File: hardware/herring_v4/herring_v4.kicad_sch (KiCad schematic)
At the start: 7 parts, among them U1 W65C02, U2 AS6C62256, U3 AT28C64B, U4 W65C51, U5 ATF16V8B, X1 CXO_DIP14, X2 CXO_DIP8

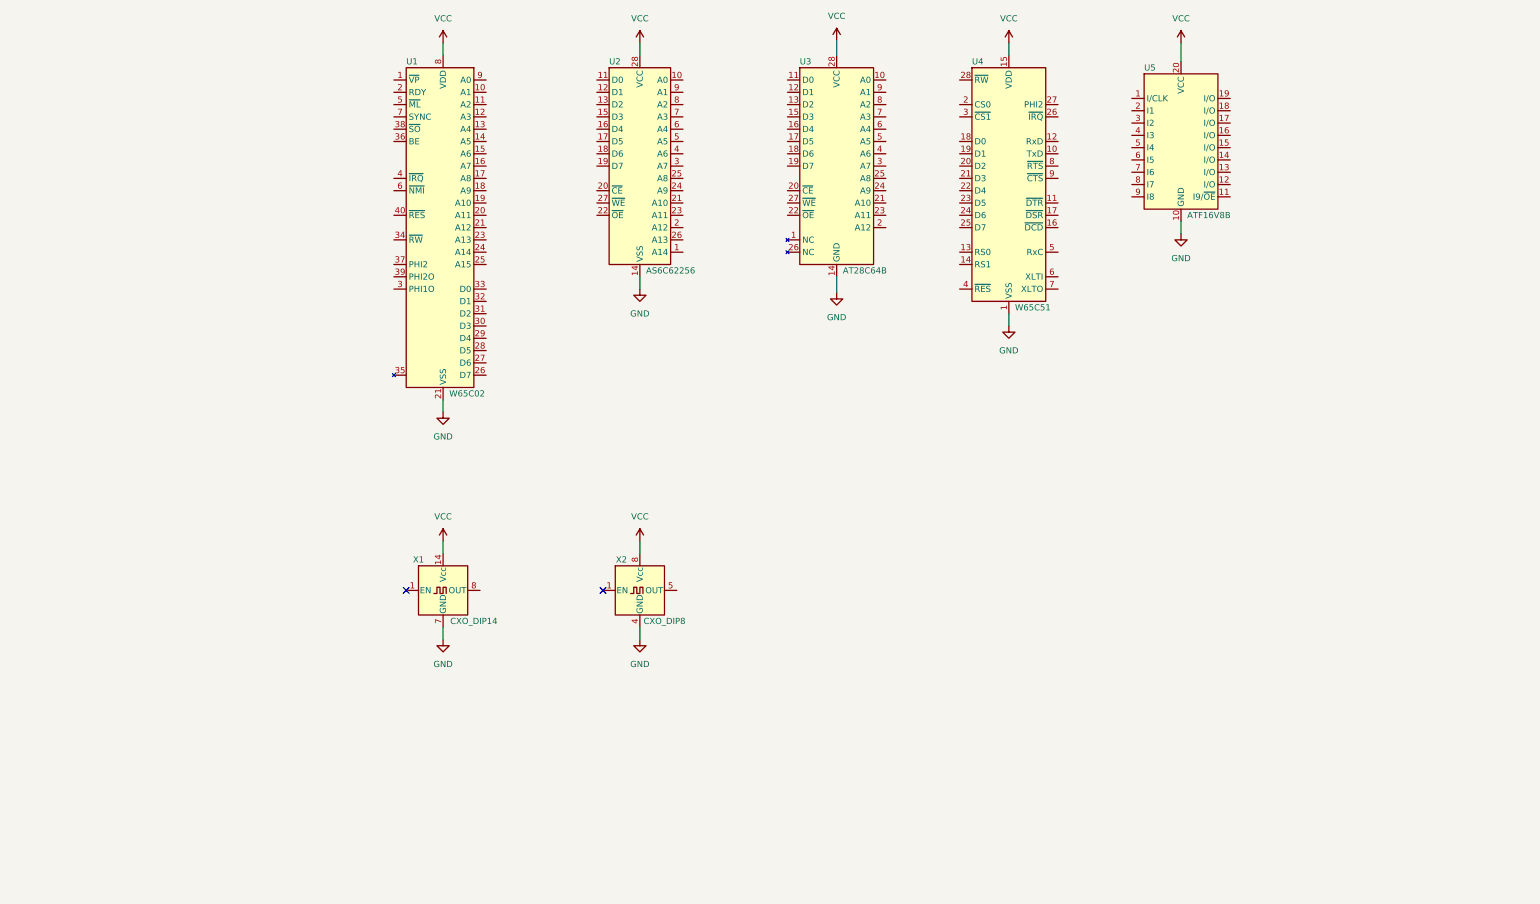
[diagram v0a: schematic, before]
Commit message: Add 16C550 to schematic
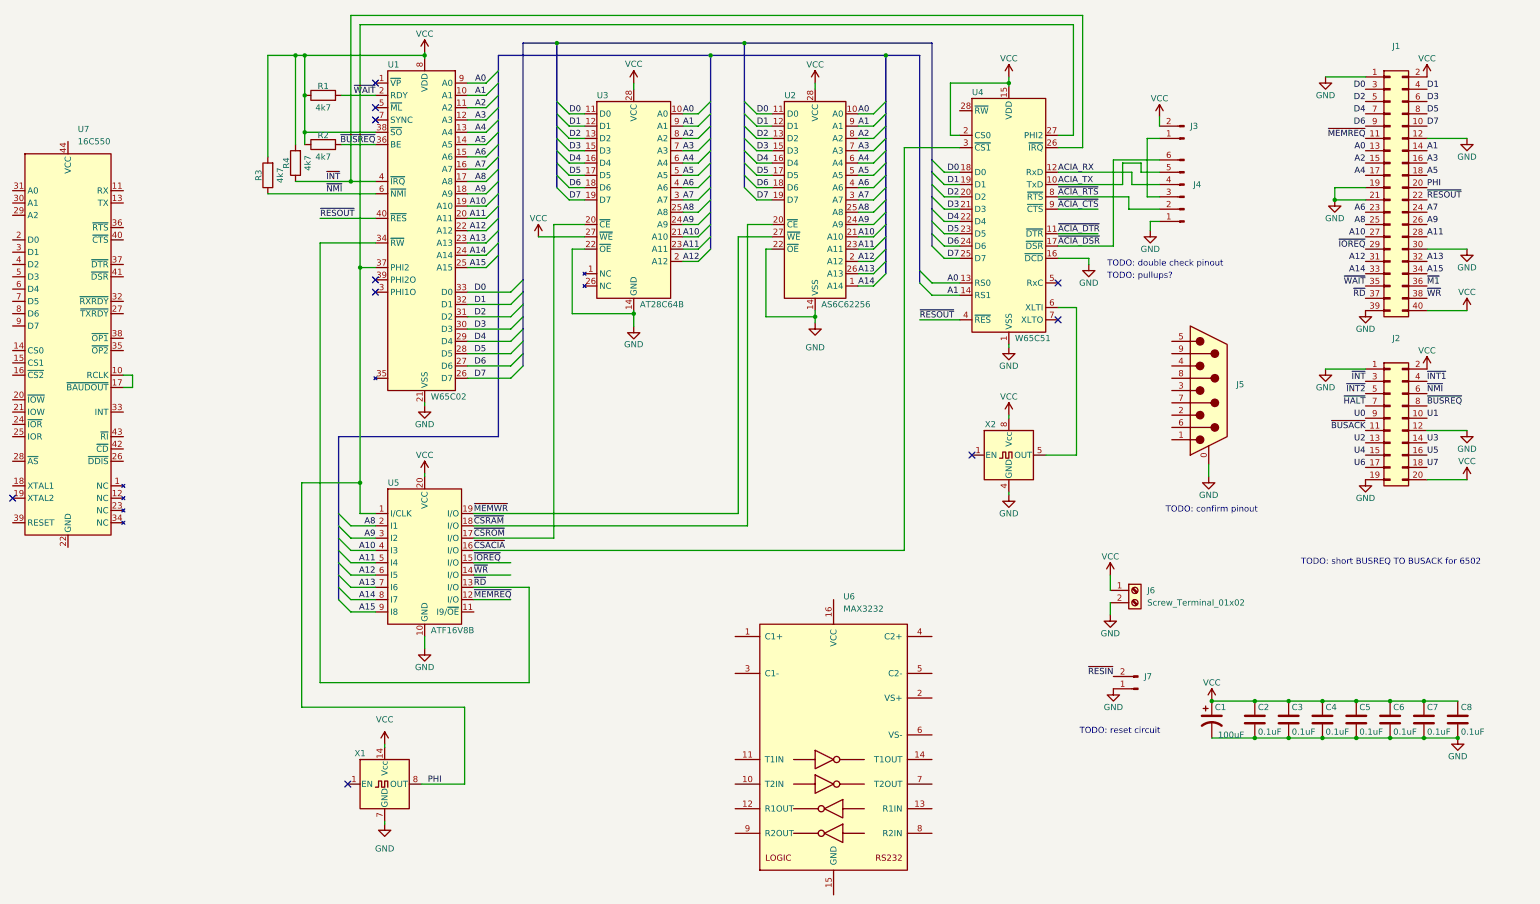
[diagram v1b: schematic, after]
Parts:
- added C1: 100uF, Capacitor_THT:CP_Radial_D8.0mm_P3.50mm, symbol Device:C_Polarized_US
- added C2, C3, C4, C5, C6, C7, C8: 0.1uF, Capacitor_THT:C_Disc_D5.0mm_W2.5mm_P5.00mm, symbol Device:C
- added J1: Conn_02x20_Odd_Even, Connector_PinSocket_2.54mm:PinSocket_2x21_P2.54mm_Horizontal, symbol Connector_Generic:Conn_02x20_Odd_Even
- added J2: Conn_02x10_Odd_Even, Connector_PinSocket_2.54mm:PinSocket_2x10_P2.54mm_Horizontal, symbol Connector_Generic:Conn_02x10_Odd_Even
- added J3, J7: Conn_01x02_Male, Connector_PinHeader_2.54mm:PinHeader_1x02_P2.54mm_Vertical, symbol Connector:Conn_01x02_Male
- added J4: Conn_01x06_Male, Connector_PinHeader_2.54mm:PinHeader_1x06_P2.54mm_Vertical, symbol Connector:Conn_01x06_Male
- added J5: DB9_Male_MountingHoles, Connector_Dsub:DSUB-9_Male_Horizontal_P2.77x2.84mm_EdgePinOffset7.70mm_Housed_MountingHolesOffset9.12mm, symbol Connector:DB9_Male_MountingHoles
- added J6: Screw_Terminal_01x02, TerminalBlock:TerminalBlock_bornier-2_P5.08mm, symbol Connector:Screw_Terminal_01x02
- added R1, R2, R3, R4: 4k7, Resistor_THT:R_Axial_DIN0207_L6.3mm_D2.5mm_P10.16mm_Horizontal, symbol Device:R
- added U6: MAX3232, Package_DIP:DIP-16_W7.62mm_Socket, symbol Interface_UART:MAX3232
- added U7: 16C550, Package_LCC:PLCC-44_THT-Socket, symbol herring:16C550
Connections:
- net GND: now also U2.22 (~{OE}), U3.22 (~{OE}), U4.16 (~{DCD}), C1.2, C2.2, C3.2, C4.2, C5.2, C6.2, C7.2, C8.2, J1.1 (Pin_1), J1.12 (Pin_12), J1.19 (Pin_19), J1.21 (Pin_21), J1.30 (Pin_30), J1.39 (Pin_39), J2.1 (Pin_1), J2.12 (Pin_12), J2.19 (Pin_19), J4.1 (Pin_1), J5.0 (PAD), J6.2 (Pin_2), J7.1 (Pin_1)
- net VCC: now also U1.38 (~{SO}), U3.27 (~{WE}), U4.2 (CS0), C1.1, C2.1, C3.1, C4.1, C5.1, C6.1, C7.1, C8.1, J1.2 (Pin_2), J1.40 (Pin_40), J2.2 (Pin_2), J2.20 (Pin_20), J3.2 (Pin_2), J6.1 (Pin_1), R1.1, R2.1, R3.2, R4.2
- net at X2.5 (OUT): now also U4.6 (XLTI)
- net PHI: now reaches U5.1 (I/CLK)
- net PHI: now also U1.37 (PHI2), U4.27 (PHI2), X1.8 (OUT), J1.20 (Pin_20)
- net ~{MEMREQ}: now reaches U5.12 (I/O)
- net ~{MEMREQ}: now also J1.11 (Pin_11)
- net ~{RD}: now reaches U5.13 (I/O)
- net ~{RD}: now also U1.34 (~{RW}), J1.37 (Pin_37)
- net ~{WR}: now reaches U5.14 (I/O)
- net ~{WR}: now also J1.38 (Pin_38)
- net ~{IOREQ}: now reaches U5.15 (I/O)
- net ~{IOREQ}: now also J1.29 (Pin_29)
- net ~{CSACIA}: now reaches U5.16 (I/O)
- net ~{CSACIA}: now also U4.3 (~{CS1})
- net ~{CSROM}: now reaches U5.17 (I/O)
- net ~{CSROM}: now also U3.20 (~{CE})
- net ~{CSRAM}: now reaches U5.18 (I/O)
- net ~{CSRAM}: now also U2.20 (~{CE})
- net ~{MEMWR}: now reaches U5.19 (I/O)
- net ~{MEMWR}: now also U2.27 (~{WE})
- net A8: now reaches U5.2 (I1)
- net A8: now also U1.17 (A8), U2.25 (A8), U3.25 (A8), J1.25 (Pin_25)
- net A9: now reaches U5.3 (I2)
- net A9: now also U1.18 (A9), U2.24 (A9), U3.24 (A9), J1.26 (Pin_26)
- net A10: now reaches U5.4 (I3)
- net A10: now also U1.19 (A10), U2.21 (A10), U3.21 (A10), J1.27 (Pin_27)
- net A11: now reaches U5.5 (I4)
- net A11: now also U1.20 (A11), U2.23 (A11), U3.23 (A11), J1.28 (Pin_28)
- net A12: now reaches U5.6 (I5)
- net A12: now also U1.22 (A12), U2.2 (A12), U3.2 (A12), J1.31 (Pin_31)
- net A13: now reaches U5.7 (I6)
- net A13: now also U1.23 (A13), U2.26 (A13), J1.32 (Pin_32)
- net A14: now reaches U5.8 (I7)
- net A14: now also U1.24 (A14), U2.1 (A14), J1.33 (Pin_33)
- net A15: now reaches U5.9 (I8)
- net A15: now also U1.25 (A15), J1.34 (Pin_34)
- net A0: now reaches U2.10 (A0)
- net A0: now also U1.9 (A0), U3.10 (A0), U4.13 (RS0), J1.13 (Pin_13)
- net D0: now reaches U2.11 (D0)
- net D0: now also U1.33 (D0), U3.11 (D0), U4.18 (D0), J1.3 (Pin_3)
- net D1: now reaches U2.12 (D1)
- net D1: now also U1.32 (D1), U3.12 (D1), U4.19 (D1), J1.4 (Pin_4)
- net D2: now reaches U2.13 (D2)
- net D2: now also U1.31 (D2), U3.13 (D2), U4.20 (D2), J1.5 (Pin_5)
- net D3: now reaches U2.15 (D3)
- net D3: now also U1.30 (D3), U3.15 (D3), U4.21 (D3), J1.6 (Pin_6)
- net D4: now reaches U2.16 (D4)
- net D4: now also U1.29 (D4), U3.16 (D4), U4.22 (D4), J1.7 (Pin_7)
- net D5: now reaches U2.17 (D5)
- net D5: now also U1.28 (D5), U3.17 (D5), U4.23 (D5), J1.8 (Pin_8)
- net D6: now reaches U2.18 (D6)
- net D6: now also U1.27 (D6), U3.18 (D6), U4.24 (D6), J1.9 (Pin_9)
- net D7: now reaches U2.19 (D7)
- net D7: now also U1.26 (D7), U3.19 (D7), U4.25 (D7), J1.10 (Pin_10)
- net A7: now reaches U2.3 (A7)
- net A7: now also U1.16 (A7), U3.3 (A7), J1.24 (Pin_24)
- net A6: now reaches U2.4 (A6)
- net A6: now also U1.15 (A6), U3.4 (A6), J1.23 (Pin_23)
- net A5: now reaches U2.5 (A5)
- net A5: now also U1.14 (A5), U3.5 (A5), J1.18 (Pin_18)
- net A4: now reaches U2.6 (A4)
- net A4: now also U1.13 (A4), U3.6 (A4), J1.17 (Pin_17)
- net A3: now reaches U2.7 (A3)
- net A3: now also U1.12 (A3), U3.7 (A3), J1.16 (Pin_16)
- net A2: now reaches U2.8 (A2)
- net A2: now also U1.11 (A2), U3.8 (A2), J1.15 (Pin_15)
- net A1: now reaches U2.9 (A1)
- net A1: now also U1.10 (A1), U3.9 (A1), U4.14 (RS1), J1.14 (Pin_14)
- net ~{WAIT}: now reaches U1.2 (RDY)
- net ~{WAIT}: now also J1.35 (Pin_35), R1.2
- net ~{BUSREQ}: now reaches U1.36 (BE)
- net ~{BUSREQ}: now also J2.8 (Pin_8), R2.2
- net ~{INT}: now reaches U1.4 (~{IRQ})
- net ~{INT}: now also U4.26 (~{IRQ}), J2.3 (Pin_3), R4.1
- net ~{RESOUT}: now reaches U1.40 (~{RES})
- net ~{RESOUT}: now also U4.4 (~{RES}), J1.22 (Pin_22)
- net ~{NMI}: now reaches U1.6 (~{NMI})
- net ~{NMI}: now also J2.6 (Pin_6), R3.1
- net ACIA_TX: now reaches U4.10 (TxD)
- net ACIA_TX: now also J4.5 (Pin_5)
- net ~{ACIA_DTR}: now reaches U4.11 (~{DTR})
- net ACIA_RX: now reaches U4.12 (RxD)
- net ACIA_RX: now also J4.4 (Pin_4)
- net ~{ACIA_DSR}: now reaches U4.17 (~{DSR})
- net ~{ACIA_DSR}: now also J4.6 (Pin_6)
- net ~{ACIA_RTS}: now reaches U4.8 (~{RTS})
- net ~{ACIA_RTS}: now also J4.2 (Pin_2)
- net ~{ACIA_CTS}: now reaches U4.9 (~{CTS})
- new net: J3.1 (Pin_1), J4.3 (Pin_3)
- new net: U7.10 (RCLK), U7.17 (~{BAUDOUT})
- new net U0: J2.9 (Pin_9)
- new net U1: J2.10 (Pin_10)
- new net U2: J2.13 (Pin_13)
- new net U3: J2.14 (Pin_14)
- new net U4: J2.15 (Pin_15)
- new net U5: J2.16 (Pin_16)
- new net U6: J2.17 (Pin_17)
- new net U7: J2.18 (Pin_18)
- new net ~{BUSACK}: J2.11 (Pin_11)
- new net ~{HALT}: J2.7 (Pin_7)
- new net ~{INT1}: J2.4 (Pin_4)
- new net ~{INT2}: J2.5 (Pin_5)
- new net ~{M1}: J1.36 (Pin_36)
- new net ~{RESIN}: J7.2 (Pin_2)
- no-connect marks 2 -> 10
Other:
- note added: "TODO: confirm pinout"
- note added: "TODO: double check pinout"
- note added: "TODO: pullups?"
- note added: "TODO: reset circuit"
- note added: "TODO: short BUSREQ TO BUSACK for 6502"
- moved on the sheet: U1, U2, U3, U4, U5, X1, X2

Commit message: Strip down CPU board schematic
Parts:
- removed J3: Conn_01x02_Male, Connector_PinHeader_2.54mm:PinHeader_1x02_P2.54mm_Vertical, symbol Connector:Conn_01x02_Male
- removed J4: Conn_01x06_Male, Connector_PinHeader_2.54mm:PinHeader_1x06_P2.54mm_Vertical, symbol Connector:Conn_01x06_Male
- removed J5: DB9_Male_MountingHoles, Connector_Dsub:DSUB-9_Male_Horizontal_P2.77x2.84mm_EdgePinOffset7.70mm_Housed_MountingHolesOffset9.12mm, symbol Connector:DB9_Male_MountingHoles
- removed J6: Screw_Terminal_01x02, TerminalBlock:TerminalBlock_bornier-2_P5.08mm, symbol Connector:Screw_Terminal_01x02
- removed U4: W65C51, Package_DIP:DIP-28_W15.24mm_Socket, symbol herring:W65C51
- removed U6: MAX3232, Package_DIP:DIP-16_W7.62mm_Socket, symbol Interface_UART:MAX3232
- removed U7: 16C550, Package_LCC:PLCC-44_THT-Socket, symbol herring:16C550
- removed X2: CXO_DIP8, Oscillator:Oscillator_DIP-8, symbol Oscillator:CXO_DIP8
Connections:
- net ~{RD}: no longer J1.37 (Pin_37)
- net ~{WR}: no longer J1.38 (Pin_38)
- net ~{CSACIA}: no longer names the net of U5.16 (I/O)
- no-connect marks 10 -> 6
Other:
- note removed: "TODO: confirm pinout"
- note removed: "TODO: double check pinout"
- note removed: "TODO: pullups?"
